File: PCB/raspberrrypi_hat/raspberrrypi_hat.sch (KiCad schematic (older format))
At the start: 18 parts, among them J3 40HAT, J6 CONN_02X02, J9 CONN_01X02, Q1 DMG2305UX, Q2 DMMT5401, U2 CAT24C32

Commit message: Start to modify Pi_HAT template to add new sheet. Create new M590 component in the library
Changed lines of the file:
@@
 $Descr A3 16535 11693
 encoding utf-8
-Sheet 1 1
+Sheet 1 2
 Title "Raspberry Pi HAT"
 Date ""
@@
 	1    0    0    -1
 $EndComp
-Text Label 3150 7400 2    60   ~ 0
-P3V3
 $Comp
 L CONN_02X02 J6
@@
 Text Label 7150 2400 2    60   ~ 0
 P5V_HAT
-Wire Wire Line
-	6400 2400 7150 2400
 Text Label 5300 2400 0    60   ~ 0
 P5V
@@
 $EndComp
 $Comp
-L GND #PWR01
+L GND #PWR4
 U 1 1 58E15A41
 P 5750 3800
-F 0 "#PWR01" H 5750 3550 50  0001 C CNN
+F 0 "#PWR4" H 5750 3550 50  0001 C CNN
 F 1 "GND" H 5750 3650 50  0000 C CNN
 F 2 "" H 5750 3800 50  0000 C CNN
@@
 $EndComp
 $Comp
-L GND #PWR02
+L GND #PWR5
 U 1 1 58E15A9E
 P 6550 3800
-F 0 "#PWR02" H 6550 3550 50  0001 C CNN
+F 0 "#PWR5" H 6550 3550 50  0001 C CNN
 F 1 "GND" H 6550 3650 50  0000 C CNN
 F 2 "" H 6550 3800 50  0000 C CNN
@@
 Connection ~ 2150 7400
 Wire Wire Line
-	2500 7400 3150 7400
+	2500 7400 3450 7400
 Wire Wire Line
 	2700 7650 2500 7650
-Connection ~ 2700 7400
 Text Label 1250 7400 0    60   ~ 0
 ID_SD_EEPROM_pu
@@
 	2100 5350 2100 5450
 $Comp
-L GND #PWR03
+L GND #PWR1
 U 1 1 58E1A612
 P 1050 5750
-F 0 "#PWR03" H 1050 5500 50  0001 C CNN
+F 0 "#PWR1" H 1050 5500 50  0001 C CNN
 F 1 "GND" H 1050 5600 50  0000 C CNN
 F 2 "" H 1050 5750 50  0000 C CNN
@@
 	1300 5850 1600 5850
 $Comp
-L GND #PWR04
+L GND #PWR2
 U 1 1 58E1AF98
 P 1050 6150
-F 0 "#PWR04" H 1050 5900 50  0001 C CNN
+F 0 "#PWR2" H 1050 5900 50  0001 C CNN
 F 1 "GND" H 1050 6000 50  0000 C CNN
 F 2 "" H 1050 6150 50  0000 C CNN
@@
 	3200 2250 4400 2250
 Wire Wire Line
-	2700 7650 2700 7400
+	2700 7400 2700 7650
 Text Notes 7150 4950 0    60   ~ 0
 HAT spec indicates to NEVER\npower the 3.3V pins on the Raspberry Pi \nfrom the HAT header. Only connect the 3.3V\npower from the Pi if the HAT does not have\n3.3V on board.\n\nIF you are designing a board that could\neither be powered by the Pi or from the HAT\nthe jumpers here can be used.\n\nIn most cases, either design the HAT \nto provide the 5V to the Pi and use the\nprotection circuit above OR power the\nHAT from the Pi and directly connect\nthe P3V3 and P5V to the P3V3_HAT and P5V_HAT\npins.
@@
 This is based on the official Raspberry Pi spec to be able to call an extension board a HAT.\nhttps://github.com/raspberrypi/hats/blob/master/designguide.md
 $Comp
-L GND #PWR05
+L GND #PWR3
 U 1 1 58E3CC10
 P 2100 6350
-F 0 "#PWR05" H 2100 6100 50  0001 C CNN
+F 0 "#PWR3" H 2100 6100 50  0001 C CNN
 F 1 "GND" H 2100 6200 50  0000 C CNN
 F 2 "" H 2100 6350 50  0000 C CNN
@@
 Wire Wire Line
 	950  6000 1550 6000
+Wire Wire Line
+	6400 2400 7150 2400
+Text Label 3150 7400 2    60   ~ 0
+P3V3
+Connection ~ 2700 7400
+$Sheet
+S 11100 2950 1850 2450
+U 59517BD0
+F0 "M590" 60
+F1 "M590.sch" 60
+$EndSheet
+Text HLabel 11100 3400 0    60   Input ~ 0
+TXD
+Text HLabel 11100 3600 0    60   Output ~ 0
+RXD
+Text HLabel 11100 4050 0    60   Output ~ 0
+RING
+Text HLabel 11100 4200 0    60   Input ~ 0
+BOOT
+Text HLabel 11100 4650 0    60   UnSpc ~ 0
+5V
+Text HLabel 11100 4900 0    60   UnSpc ~ 0
+GND
 $EndSCHEMATC

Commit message: Change Pi HAT footprints to SMD 1206_HandSoldering
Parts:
- R11, R7, R9: footprint Resistors_SMD:R_0805_HandSoldering -> Resistors_SMD:R_1206_HandSoldering
- R23, R24, R29, R6, R8: footprint Resistors_SMD:R_0603_HandSoldering -> Resistors_SMD:R_1206_HandSoldering
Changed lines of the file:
@@
 F 0 "R23" V 5830 3600 50  0000 C CNN
 F 1 "22" V 5750 3600 50  0000 C CNN
-F 2 "Resistors_SMD:R_0603_HandSoldering" V 5680 3600 50  0001 C CNN
+F 2 "Resistors_SMD:R_1206_HandSoldering" V 5680 3600 50  0001 C CNN
 F 3 "" H 5750 3600 50  0001 C CNN
 F 4 "Yageo" H -9800 -10750 50  0001 C CNN "MFR"
@@
 F 0 "R24" V 6630 3600 50  0000 C CNN
 F 1 "22" V 6550 3600 50  0000 C CNN
-F 2 "Resistors_SMD:R_0603_HandSoldering" V 6480 3600 50  0001 C CNN
+F 2 "Resistors_SMD:R_1206_HandSoldering" V 6480 3600 50  0001 C CNN
 F 3 "" H 6550 3600 50  0001 C CNN
 F 4 "Yageo" H -9000 -10950 50  0001 C CNN "MFR"
@@
 F 0 "R6" V 2430 7400 50  0000 C CNN
 F 1 "3.9K" V 2350 7400 50  0000 C CNN
-F 2 "Resistors_SMD:R_0603_HandSoldering" V 2280 7400 50  0001 C CNN
+F 2 "Resistors_SMD:R_1206_HandSoldering" V 2280 7400 50  0001 C CNN
 F 3 "" H 2350 7400 50  0001 C CNN
 F 4 "Yageo" H -13200 -6950 50  0001 C CNN "MFR"
@@
 F 0 "R8" V 2430 7650 50  0000 C CNN
 F 1 "3.9K" V 2350 7650 50  0000 C CNN
-F 2 "Resistors_SMD:R_0603_HandSoldering" V 2280 7650 50  0001 C CNN
+F 2 "Resistors_SMD:R_1206_HandSoldering" V 2280 7650 50  0001 C CNN
 F 3 "" H 2350 7650 50  0001 C CNN
 F 4 "Yageo" H -13200 -6700 50  0001 C CNN "MFR"
@@
 F 0 "R29" V 1630 6250 50  0000 C CNN
 F 1 "10K" V 1550 6250 50  0000 C CNN
-F 2 "Resistors_SMD:R_0603_HandSoldering" V 1480 6250 50  0001 C CNN
+F 2 "Resistors_SMD:R_1206_HandSoldering" V 1480 6250 50  0001 C CNN
 F 3 "" H 1550 6250 50  0001 C CNN
 F 4 "Yageo" H -14000 -8100 50  0001 C CNN "MFR"
@@
 F 0 "R7" V 6180 4300 50  0000 C CNN
 F 1 "DNP" V 6100 4300 50  0000 C CNN
-F 2 "Resistors_SMD:R_0805_HandSoldering" V 6030 4300 50  0001 C CNN
+F 2 "Resistors_SMD:R_1206_HandSoldering" V 6030 4300 50  0001 C CNN
 F 3 "" H 6100 4300 50  0001 C CNN
 F 4 "Yageo" H -9450 -10050 50  0001 C CNN "MFR"
@@
 F 0 "R9" V 6180 4950 50  0000 C CNN
 F 1 "DNP" V 6100 4950 50  0000 C CNN
-F 2 "Resistors_SMD:R_0805_HandSoldering" V 6030 4950 50  0001 C CNN
+F 2 "Resistors_SMD:R_1206_HandSoldering" V 6030 4950 50  0001 C CNN
 F 3 "" H 6100 4950 50  0001 C CNN
 F 4 "Yageo" H -9450 -9400 50  0001 C CNN "MFR"
@@
 F 0 "R11" V 1380 6100 50  0000 C CNN
 F 1 "DNP" V 1300 6100 50  0000 C CNN
-F 2 "Resistors_SMD:R_0805_HandSoldering" V 1230 6100 50  0001 C CNN
+F 2 "Resistors_SMD:R_1206_HandSoldering" V 1230 6100 50  0001 C CNN
 F 3 "" H 1300 6100 50  0001 C CNN
 F 4 "Yageo" H -14250 -8250 50  0001 C CNN "MFR"

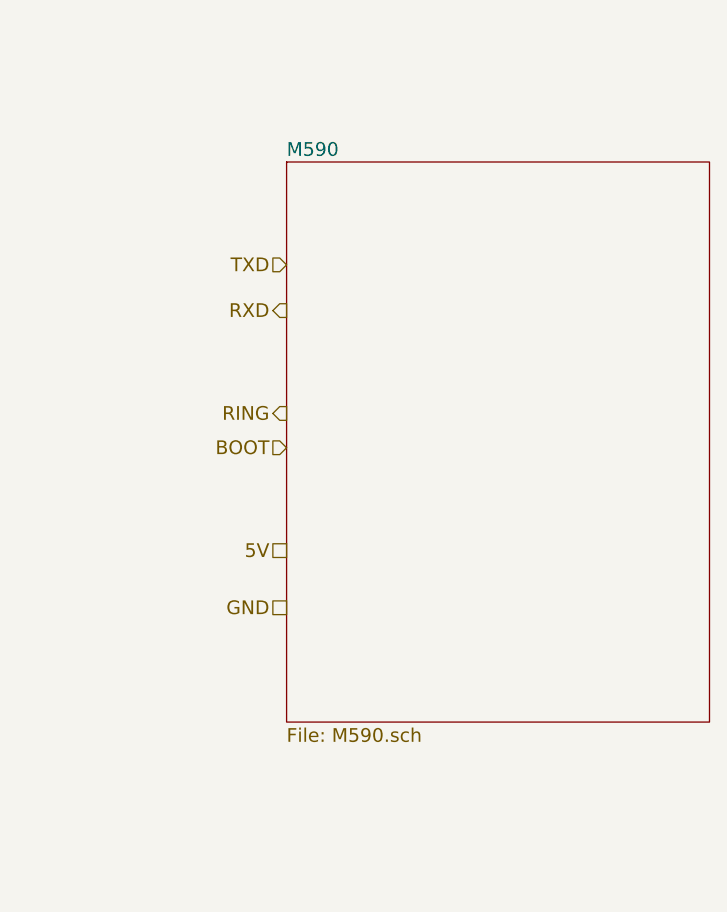
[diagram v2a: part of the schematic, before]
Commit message: Connect hierarchical sheets
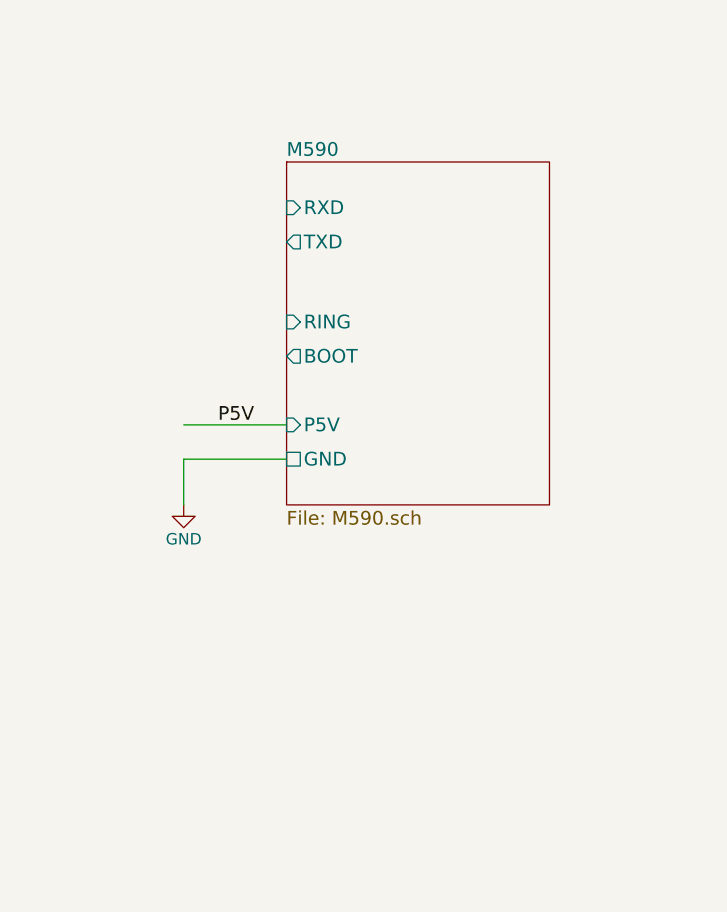
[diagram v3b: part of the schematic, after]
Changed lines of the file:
@@
 $EndComp
 $Comp
-L GND #PWR4
+L GND #PWR01
 U 1 1 58E15A41
 P 5750 3800
-F 0 "#PWR4" H 5750 3550 50  0001 C CNN
+F 0 "#PWR01" H 5750 3550 50  0001 C CNN
 F 1 "GND" H 5750 3650 50  0000 C CNN
 F 2 "" H 5750 3800 50  0000 C CNN
@@
 $EndComp
 $Comp
-L GND #PWR5
+L GND #PWR02
 U 1 1 58E15A9E
 P 6550 3800
-F 0 "#PWR5" H 6550 3550 50  0001 C CNN
+F 0 "#PWR02" H 6550 3550 50  0001 C CNN
 F 1 "GND" H 6550 3650 50  0000 C CNN
 F 2 "" H 6550 3800 50  0000 C CNN
@@
 	2100 5350 2100 5450
 $Comp
-L GND #PWR1
+L GND #PWR03
 U 1 1 58E1A612
 P 1050 5750
-F 0 "#PWR1" H 1050 5500 50  0001 C CNN
+F 0 "#PWR03" H 1050 5500 50  0001 C CNN
 F 1 "GND" H 1050 5600 50  0000 C CNN
 F 2 "" H 1050 5750 50  0000 C CNN
@@
 	1300 5850 1600 5850
 $Comp
-L GND #PWR2
+L GND #PWR04
 U 1 1 58E1AF98
 P 1050 6150
-F 0 "#PWR2" H 1050 5900 50  0001 C CNN
+F 0 "#PWR04" H 1050 5900 50  0001 C CNN
 F 1 "GND" H 1050 6000 50  0000 C CNN
 F 2 "" H 1050 6150 50  0000 C CNN
@@
 This is based on the official Raspberry Pi spec to be able to call an extension board a HAT.\nhttps://github.com/raspberrypi/hats/blob/master/designguide.md
 $Comp
-L GND #PWR3
+L GND #PWR05
 U 1 1 58E3CC10
 P 2100 6350
-F 0 "#PWR3" H 2100 6100 50  0001 C CNN
+F 0 "#PWR05" H 2100 6100 50  0001 C CNN
 F 1 "GND" H 2100 6200 50  0000 C CNN
 F 2 "" H 2100 6350 50  0000 C CNN
@@
 P3V3
 Connection ~ 2700 7400
+Wire Wire Line
+	10650 4250 11100 4250
+Text Label 10800 4100 0    60   ~ 0
+P5V
+Wire Wire Line
+	10650 4250 10650 4450
+$Comp
+L GND #PWR06
+U 1 1 5952BEE9
+P 10650 4450
+F 0 "#PWR06" H 10650 4200 50  0001 C CNN
+F 1 "GND" H 10650 4300 50  0000 C CNN
+F 2 "" H 10650 4450 50  0000 C CNN
+F 3 "" H 10650 4450 50  0000 C CNN
+	1    10650 4450
+	1    0    0    -1
+$EndComp
+Wire Wire Line
+	11100 4100 10650 4100
 $Sheet
-S 11100 2950 1850 2450
+S 11100 2950 1150 1500
 U 59517BD0
 F0 "M590" 60
 F1 "M590.sch" 60
+F2 "P5V" I L 11100 4100 60
+F3 "TXD" O L 11100 3300 60
+F4 "RXD" I L 11100 3150 60
+F5 "RING" I L 11100 3650 60
+F6 "BOOT" O L 11100 3800 60
+F7 "GND" U L 11100 4250 60
 $EndSheet
-Text HLabel 11100 3400 0    60   Input ~ 0
-TXD
-Text HLabel 11100 3600 0    60   Output ~ 0
-RXD
-Text HLabel 11100 4050 0    60   Output ~ 0
-RING
-Text HLabel 11100 4200 0    60   Input ~ 0
-BOOT
-Text HLabel 11100 4650 0    60   UnSpc ~ 0
-5V
-Text HLabel 11100 4900 0    60   UnSpc ~ 0
-GND
 $EndSCHEMATC

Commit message: SCH: M590 and pi wirering
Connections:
- net TXD: now reaches J3.10 (BCM15)
- net RXD: now reaches J3.8 (BCM14)
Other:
- note added: "(Pi RXD0)"
- note added: "(Pi TXD0)"
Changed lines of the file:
@@
 Wire Wire Line
 	10650 4250 11100 4250
-Text Label 10800 4100 0    60   ~ 0
+Text Label 10650 4100 0    60   ~ 0
 P5V
 Wire Wire Line
@@
 F7 "GND" U L 11100 4250 60
 $EndSheet
+Wire Wire Line
+	3200 2550 4400 2550
+Wire Wire Line
+	3200 2650 4400 2650
+Wire Wire Line
+	10650 3150 11100 3150
+Wire Wire Line
+	11100 3300 10650 3300
+Text Label 10650 3150 0    60   ~ 0
+RXD
+Text Label 10650 3300 0    60   ~ 0
+TXD
+Text Label 4400 2550 2    60   ~ 0
+RXD
+Text Label 4400 2650 2    60   ~ 0
+TXD
+Text Notes 3200 2550 0    60   ~ 0
+(Pi TXD0)
+Text Notes 3200 2650 0    60   ~ 0
+(Pi RXD0)
 $EndSCHEMATC

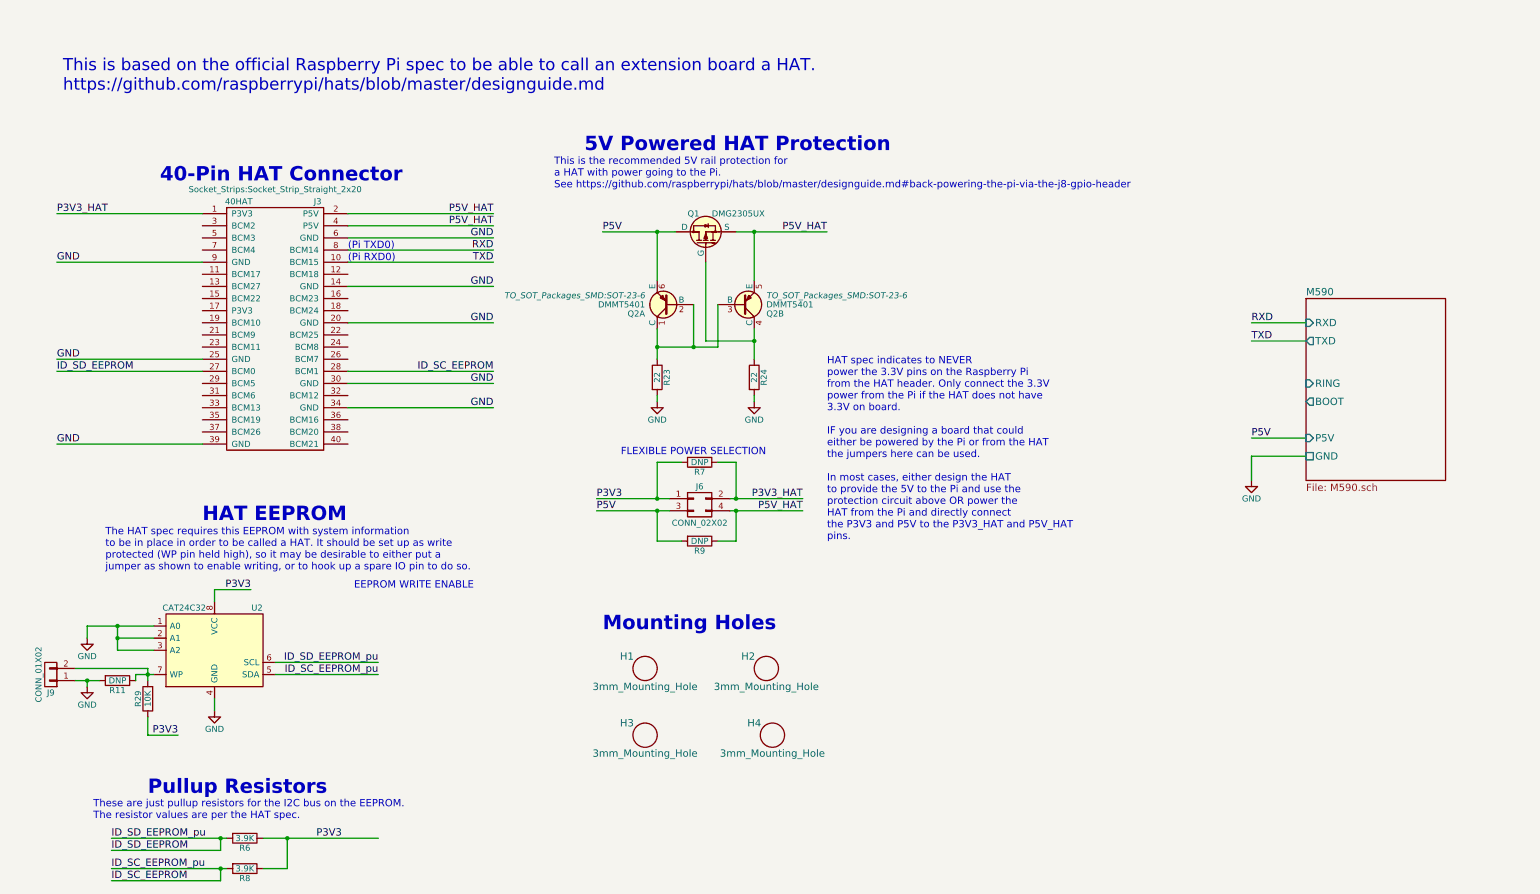
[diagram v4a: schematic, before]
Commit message: SCH: Change page size to A4, update footer and add comments about parts
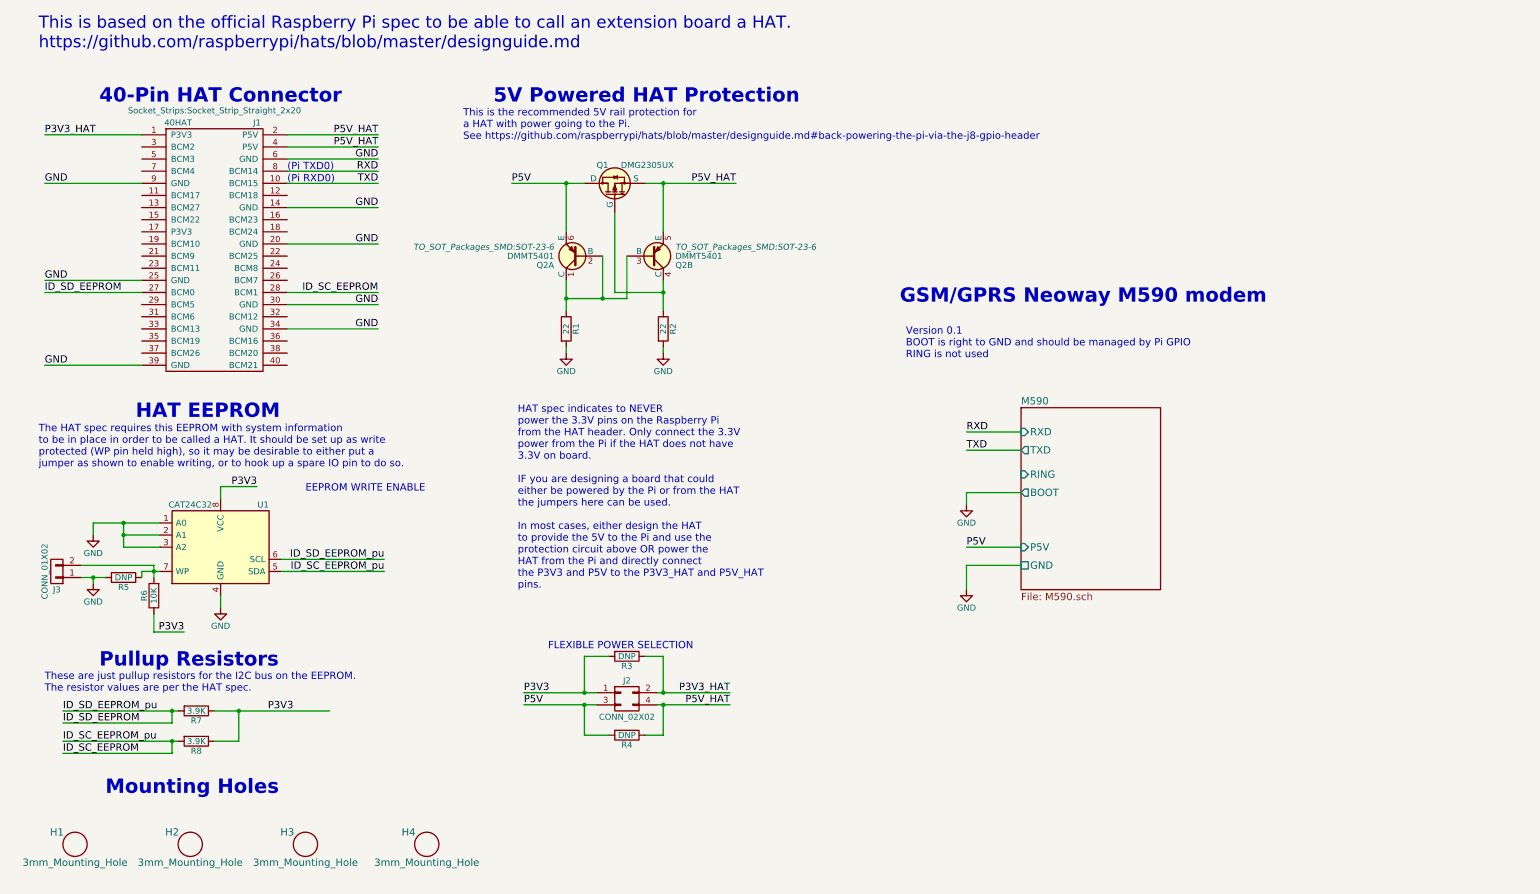
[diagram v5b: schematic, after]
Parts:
- renumbered J3 to J1, J6 to J2, J9 to J3, R23 to R1, R24 to R2, R7 to R3, R9 to R4, R11 to R5, R29 to R6, R6 to R7, U2 to U1
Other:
- note added: "GSM/GPRS Neoway M590 modem"
- note added: "Version 0.1\nBOOT is right to GND and should be managed by Pi GPIO\nRING is not used"
- moved on the sheet: H1, H2, H3, H4, J1, J2, J3, Q1, Q2A, Q2B, R1, R2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
